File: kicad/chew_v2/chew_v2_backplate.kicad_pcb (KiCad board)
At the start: 2 copper layers, 160.3 x 91.9 mm, 14 parts

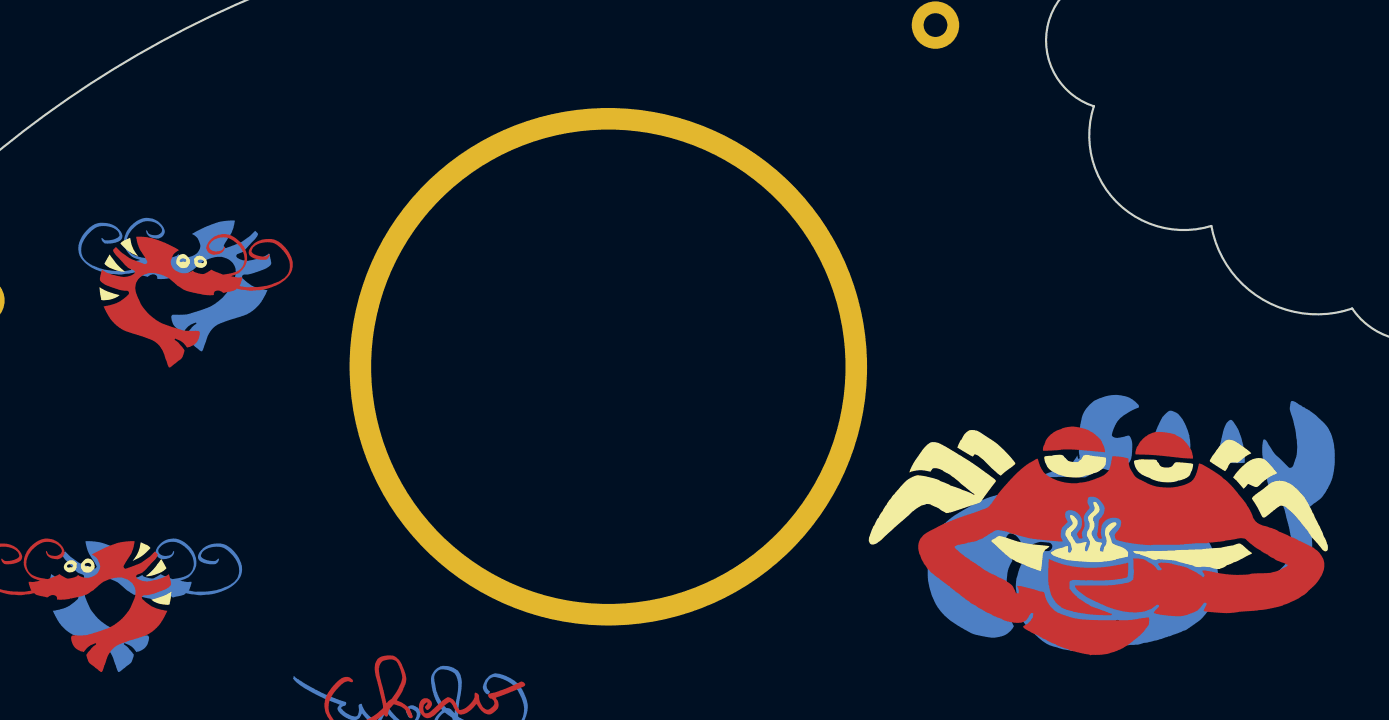
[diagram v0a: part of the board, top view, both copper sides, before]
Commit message: Up backplates with buzzer holes
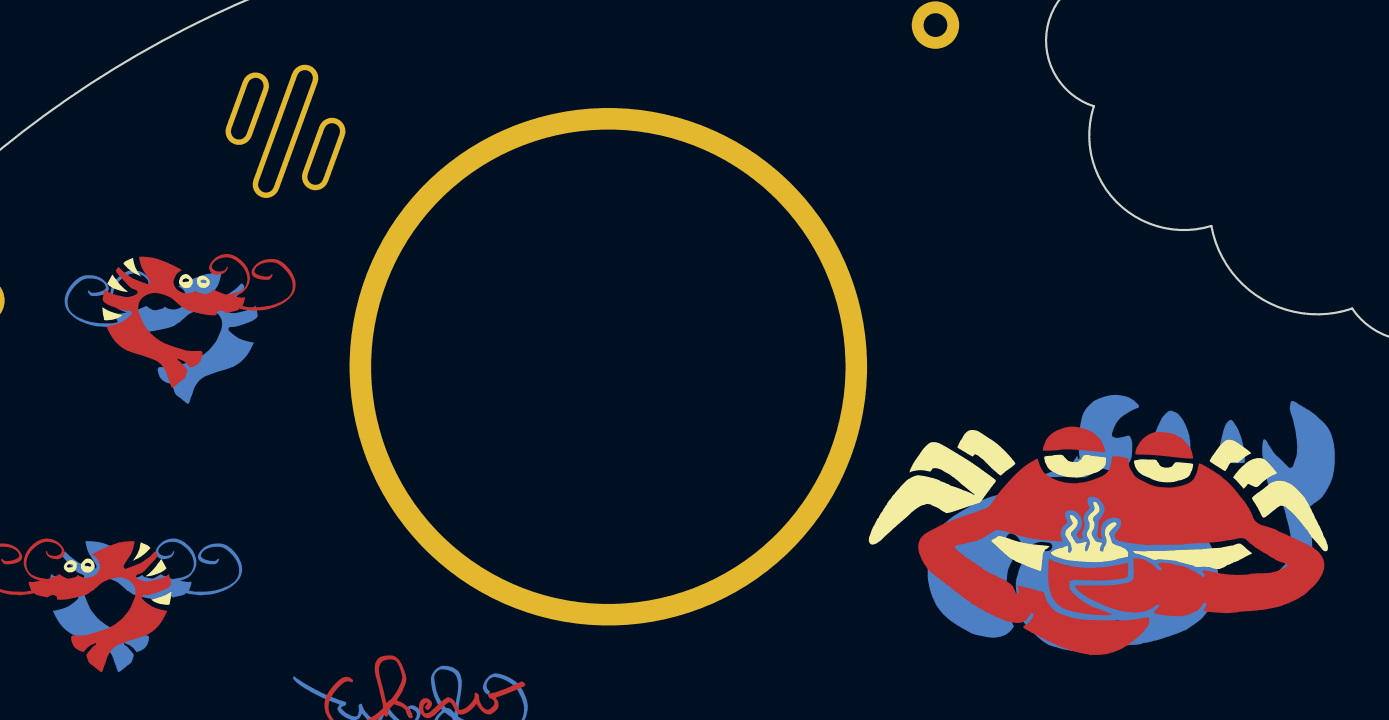
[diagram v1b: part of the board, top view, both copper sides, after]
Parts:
- added ?: , , F.Cu at (82.1, 74.5)
- added ?: , , F.Cu at (75.0, 70.3)
- added ?: , , F.Cu at (78.5, 72.4)
- moved G*** 5.02 mm to (67.7, 89.9)
- moved G*** 1.88 mm to (69.8, 88.4)
